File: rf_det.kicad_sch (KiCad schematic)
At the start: 16 parts, among them U2 AD8318ACPZ-REEL7, U3 AD8318ACPZ-REEL7

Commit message: PN update
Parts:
- FB4: PN (none) -> BLM18KG601SH1D
- R36, R38: PN RS73G1JRTTD52R3B -> CR0603-FX-52R3ELF
- R37, R39: PN (none) -> CRCW0603499RFKEA
- U2, U3: value AD8318ACPZ-REEL7 -> AD8318; PN (none) -> AD8318ACPZ-REEL7
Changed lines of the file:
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@@
       (effects (font (size 1.27 1.27)) hide)
     )
-    (property "PN" "" (at 123.19 203.2 90)
+    (property "PN" "BLM18KG601SH1D" (at 123.19 203.2 90)
       (effects (font (size 1.27 1.27)) hide)
     )
@@
       (effects (font (size 1.27 1.27)))
     )
-    (property "Value" "AD8318ACPZ-REEL7" (at 128.27 111.76 0)
+    (property "Value" "AD8318" (at 128.27 111.76 0)
       (effects (font (size 1.27 1.27)))
     )
@@
     (property "Manufacturer_Part_Number" "AD8318ACPZ-REEL7" (at 142.24 888.9 0)
       (effects (font (size 1.27 1.27)) (justify left top) hide)
+    )
+    (property "PN" " AD8318ACPZ-REEL7 " (at 110.49 101.6 0)
+      (effects (font (size 1.27 1.27)) hide)
     )
     (pin "1")
@@
       (effects (font (size 1.27 1.27)) hide)
     )
-    (property "PN" "" (at 152.4 106.68 0)
+    (property "PN" "CRCW0603499RFKEA" (at 152.4 106.68 0)
       (effects (font (size 1.27 1.27)) hide)
     )
@@
       (effects (font (size 1.27 1.27)))
     )
-    (property "Value" "AD8318ACPZ-REEL7" (at 316.6495 97.2698 0)
+    (property "Value" "AD8318" (at 316.6495 97.2698 0)
       (effects (font (size 1.27 1.27)))
     )
@@
     (property "Manufacturer_Part_Number" "AD8318ACPZ-REEL7" (at 307.34 888.9 0)
       (effects (font (size 1.27 1.27)) (justify left top) hide)
+    )
+    (property "PN" " AD8318ACPZ-REEL7 " (at 275.59 101.6 0)
+      (effects (font (size 1.27 1.27)) hide)
     )
     (pin "1")
@@
       (effects (font (size 1.27 1.27)) hide)
     )
-    (property "PN" "RS73G1JRTTD52R3B" (at 294.64 67.31 0)
+    (property "PN" " CR0603-FX-52R3ELF " (at 294.64 67.31 0)
       (effects (font (size 1.27 1.27)) hide)
     )
@@
       (effects (font (size 1.27 1.27)) hide)
     )
-    (property "PN" "RS73G1JRTTD52R3B" (at 129.54 67.31 0)
+    (property "PN" " CR0603-FX-52R3ELF " (at 129.54 67.31 0)
       (effects (font (size 1.27 1.27)) hide)
     )
@@
       (effects (font (size 1.27 1.27)) hide)
     )
-    (property "PN" "" (at 317.5 106.68 0)
-      (effects (font (size 1.27 1.27)) hide)
-    )
+    (property "PN" "CRCW0603499RFKEA" (at 317.5 106.68 0)
+      (effects (font (size 1.27 1.27)) hide)
+    )

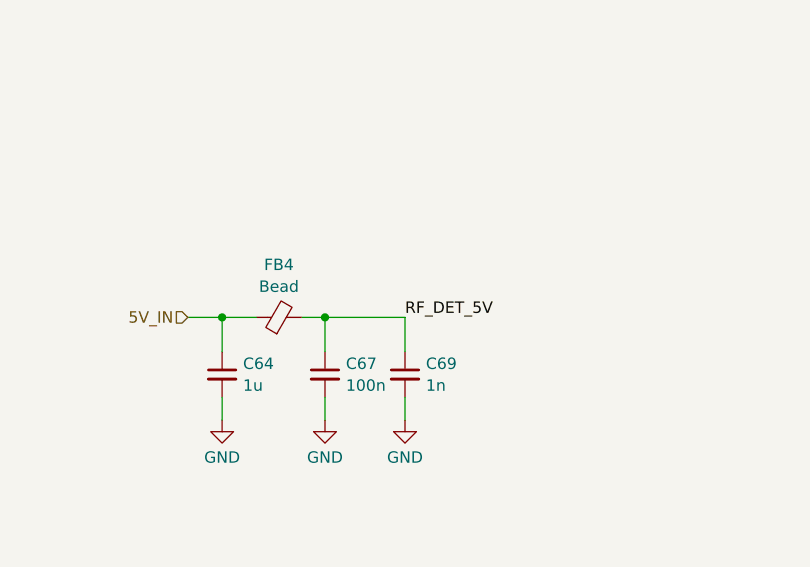
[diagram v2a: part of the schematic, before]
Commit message: `PWR_FLAG`, ERC cleanup
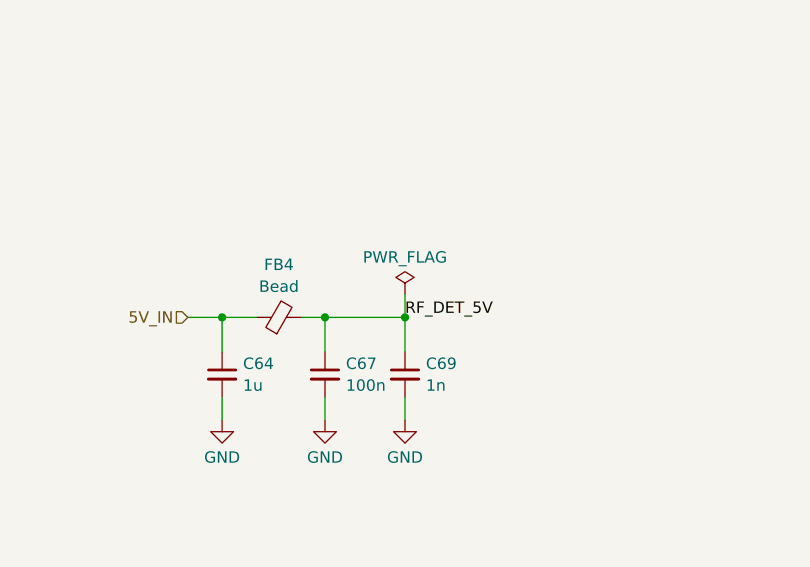
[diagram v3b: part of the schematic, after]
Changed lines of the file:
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@@
   (junction (at 323.85 106.68) (diameter 0) (color 0 0 0 0)
+  )
+  (junction (at 137.16 203.2) (diameter 0) (color 0 0 0 0)
   )
   (junction (at 107.95 109.22) (diameter 0) (color 0 0 0 0)
@@
   )
   (wire (pts (xy 128.27 78.74) (xy 128.27 86.36))
+    (stroke (width 0) (type default))
+  )
+  (wire (pts (xy 137.16 200.66) (xy 137.16 203.2))
     (stroke (width 0) (type default))
   )
@@
         )
       )
+    )
+  )
+  (symbol (lib_id "power:PWR_FLAG") (at 137.16 200.66 0) (unit 1)
+    (in_bom yes) (on_board yes) (dnp no) (fields_autoplaced)
+    (property "Reference" "#FLG01" (at 137.16 198.755 0)
+      (effects (font (size 1.27 1.27)) hide)
+    )
+    (property "Value" "PWR_FLAG" (at 137.16 196.5269 0)
+      (effects (font (size 1.27 1.27)))
+    )
+    (property "Footprint" "" (at 137.16 200.66 0)
+      (effects (font (size 1.27 1.27)) hide)
+    )
+    (property "Datasheet" "~" (at 137.16 200.66 0)
+      (effects (font (size 1.27 1.27)) hide)
+    )
+    (pin "1")
+    (instances
+      (project "m17-rru-rf"
+        (path "/4c42207c-9e6b-42da-ad38-da126b892014/270fa747-1697-46c9-b996-5c9733c883e2"
+          (reference "#FLG01") (unit 1)
+        )
+        (path "/4c42207c-9e6b-42da-ad38-da126b892014/ccc39fee-262d-4ac9-a9a6-59e024db6eed"
+          (reference "#FLG06") (unit 1)
+        )
+      )

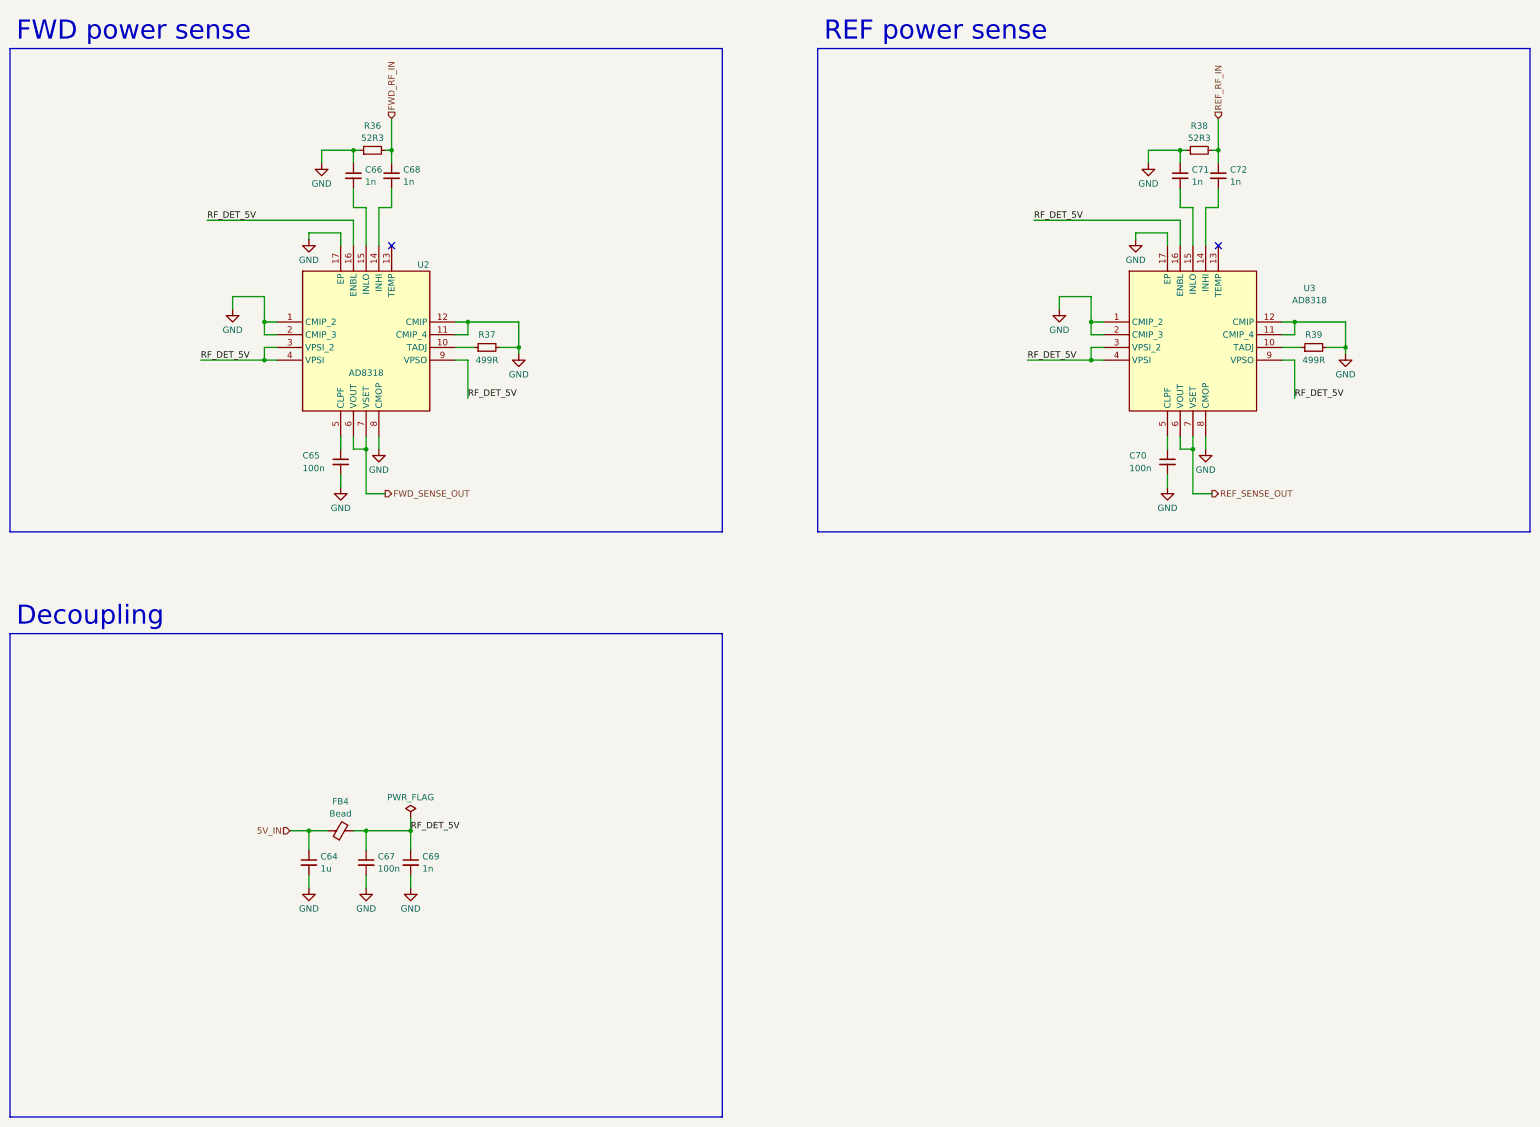
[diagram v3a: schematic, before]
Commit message: TP updates, temp sensor added
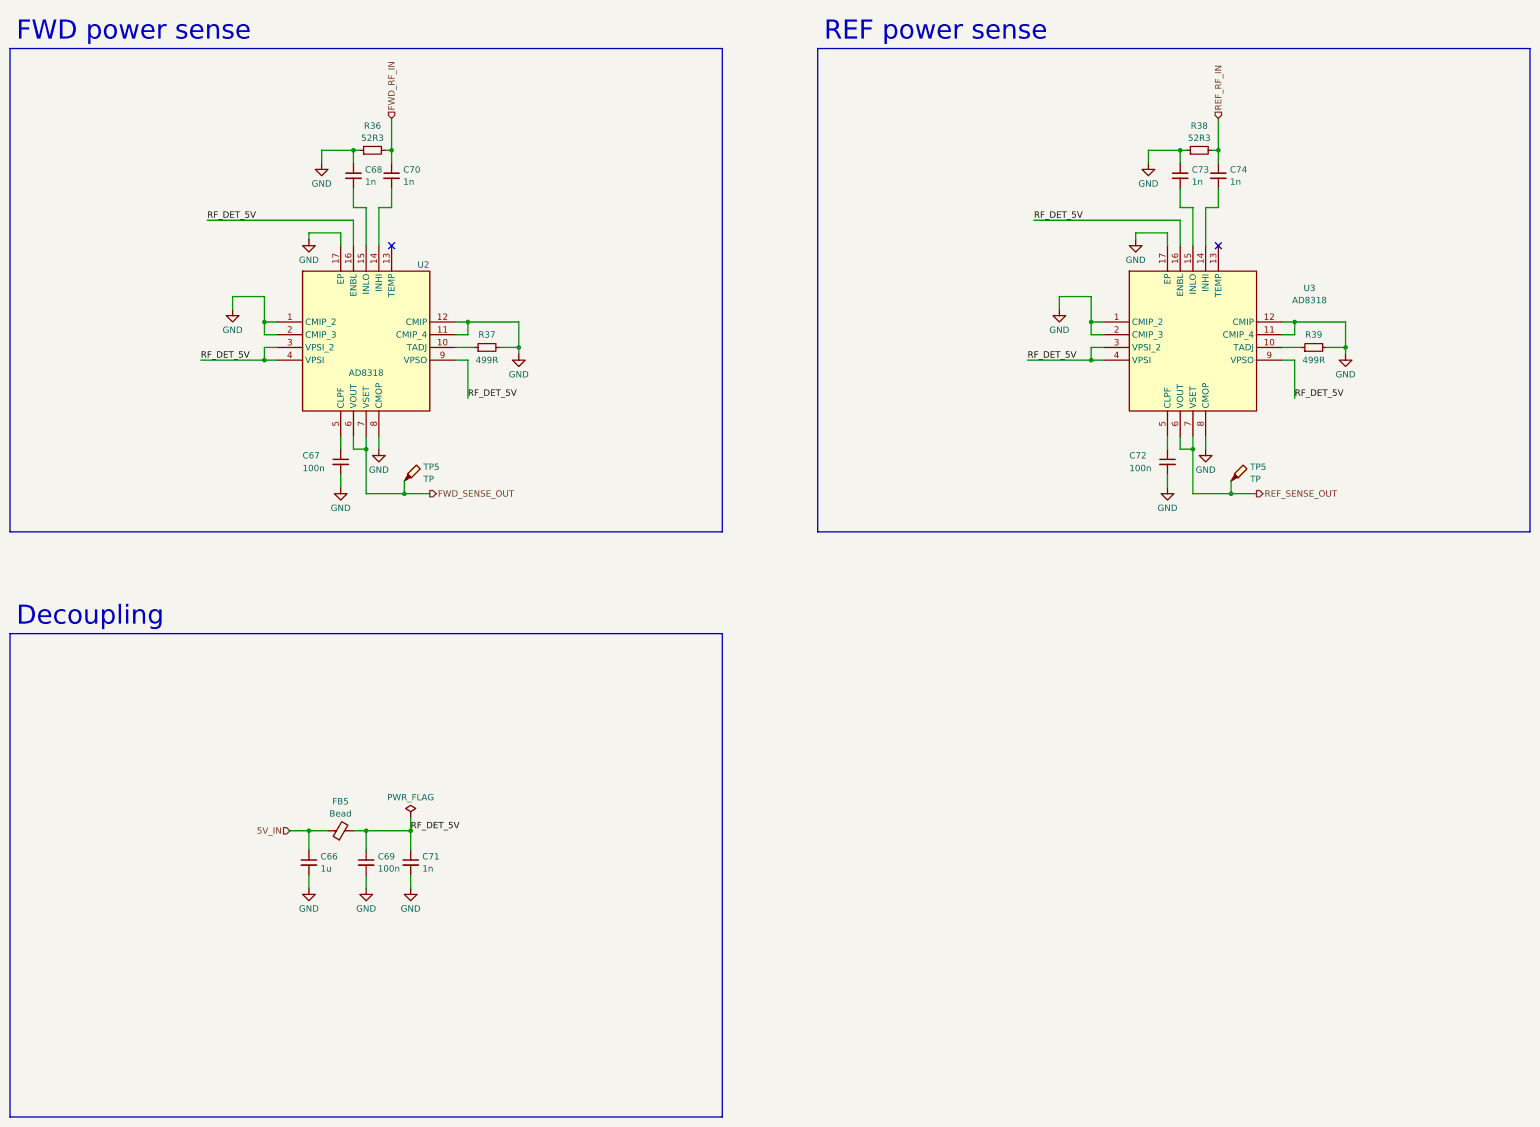
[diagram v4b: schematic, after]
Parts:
- added TP5 (x2): TP, TestPoint:TestPoint_Pad_D1.5mm, symbol Connector:TestPoint_Probe
- renumbered C64 to C66, C65 to C67, C66 to C68, C67 to C69, C68 to C70, C69 to C71, C70 to C72, C71 to C73, C72 to C74, FB4 to FB5
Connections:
- net FWD_SENSE_OUT: now also TP5.1
- net REF_SENSE_OUT: now also TP5.1

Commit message: date update
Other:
- title: M17 Remote Radio Unit - RF board -> Remote Radio Unit - RF board
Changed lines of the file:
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@@
   (paper "A3")
   (title_block
-    (title "M17 Remote Radio Unit - RF board")
-    (date "28-10-2023")
+    (title "Remote Radio Unit - RF board")
+    (date "30-10-2023")
     (rev "A")
     (company "M17 Project")
